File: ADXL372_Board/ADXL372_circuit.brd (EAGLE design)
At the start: 45 x 45 mm, 35 parts, among them IC4 SI7006-A20-IM, IC5 LP5907MFX-2.5/NOPB, SW1 DHT-4235A, U1 MX25R1635FM1IL0, U2 ADXL345BCCZ, U3 ADXL372BCCZ-RL7, Y1 16MHZ_X053201602002, Y2 3.2768KHZ

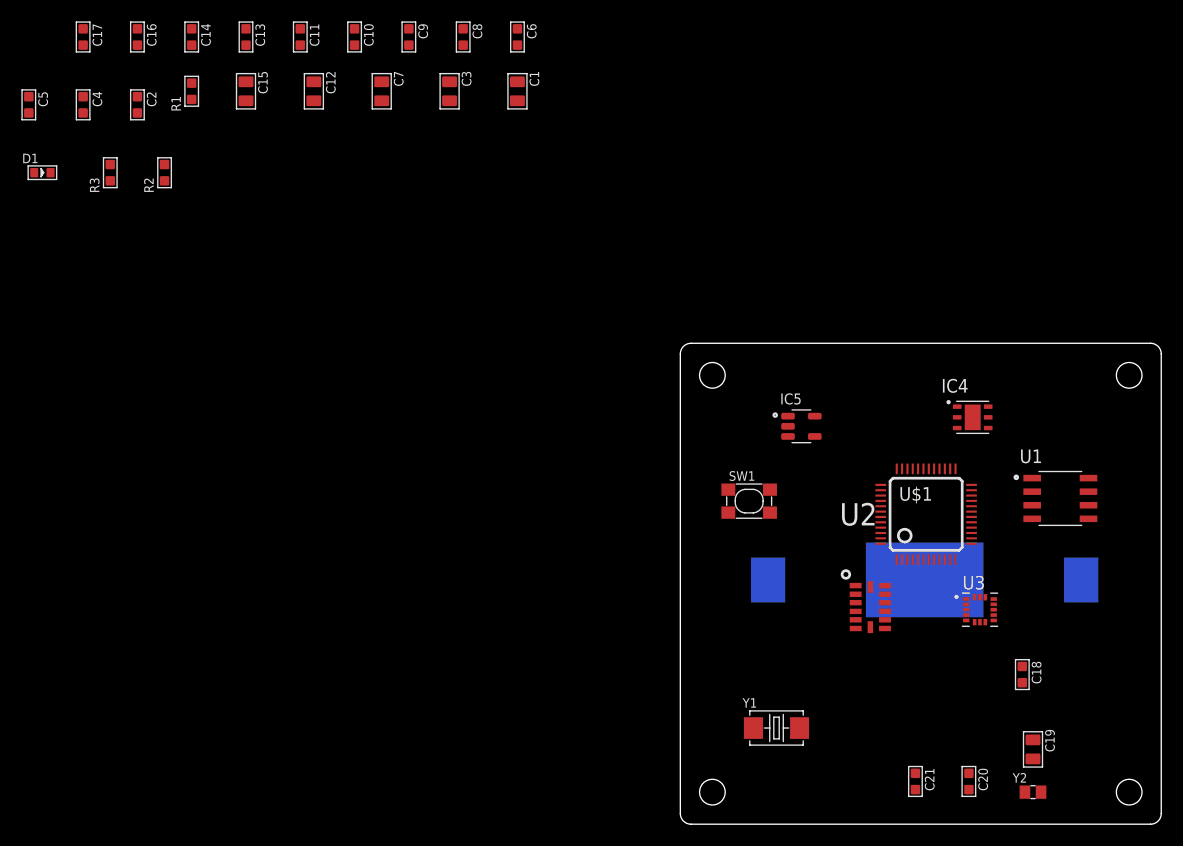
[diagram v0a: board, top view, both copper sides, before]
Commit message: 基板図面を修正
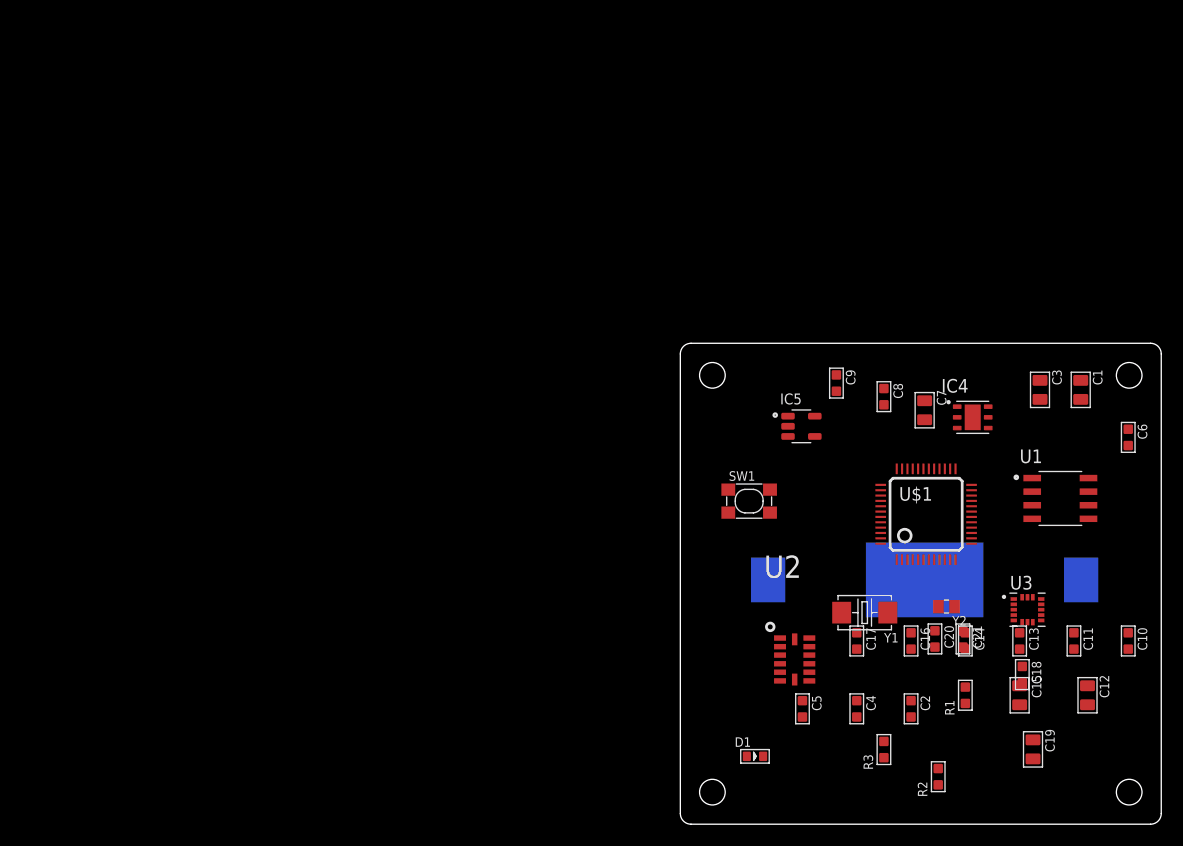
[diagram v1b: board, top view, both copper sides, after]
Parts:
- moved C10 91.8 mm to (41.9, 17.1)
- moved C11 91.8 mm to (36.8, 17.1)
- moved C12 91.8 mm to (38.1, 12.1)
- moved C13 91.8 mm to (31.8, 17.1)
- moved C14 91.8 mm to (26.7, 17.1)
- moved C15 91.8 mm to (31.8, 12.1)
- moved C16 91.8 mm to (21.6, 17.1)
- moved C17 91.8 mm to (16.5, 17.1)
- moved C2 91.8 mm to (21.6, 10.8)
- moved C4 91.8 mm to (16.5, 10.8)
- moved C5 91.8 mm to (11.4, 10.8)
- moved R1 91.8 mm to (26.7, 12.1)
- moved R2 91.8 mm to (24.1, 4.45)
- moved R3 90.3 mm to (19.1, 6.99)
- moved D1 86.2 mm to (6.99, 6.35)
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
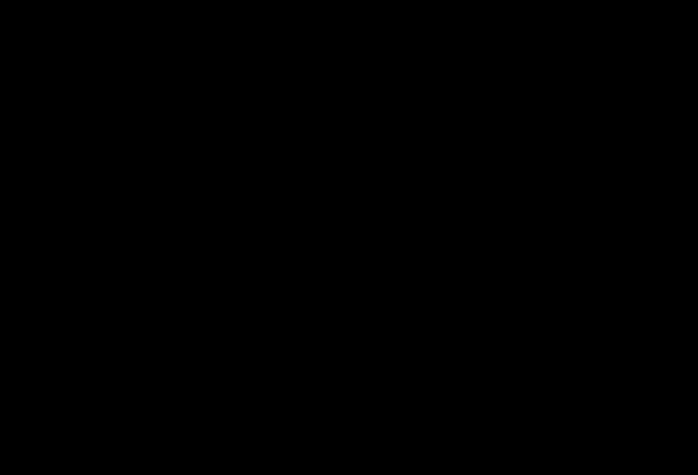
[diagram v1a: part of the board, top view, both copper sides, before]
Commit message: LED駆動用FETを追加
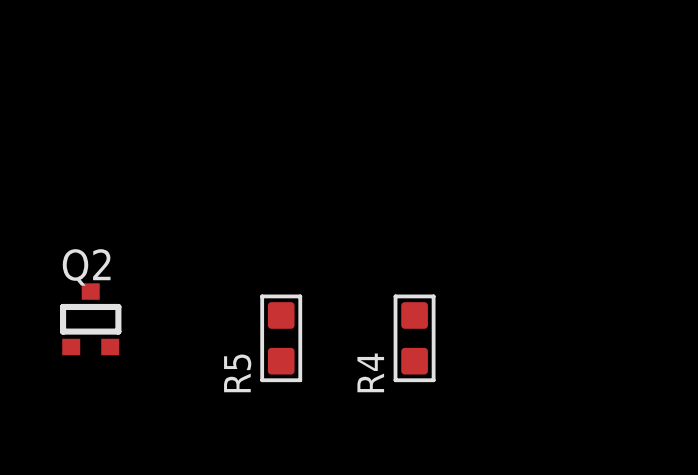
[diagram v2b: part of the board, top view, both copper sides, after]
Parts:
- added Q2: BSS138W, BSS138W:SOT323-R
- added R4: 100k, OPL_Resistor:R0603
- added R5: 100, OPL_Resistor:R0603
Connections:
- new net N$17: R5.2, U$1.10
- new net N$20: Q2.1, R4.2, R5.1
- new net VCC: C15.2, C7.2, IC5.5
- net +2V5: no longer C15.2, C7.2, IC5.5
- net +3V3: now also R1.2
- net GND: now also Q2.2, R4.1; no longer D1.-
- net N$19: now also D1.-, Q2.3; no longer R1.2, U$1.10

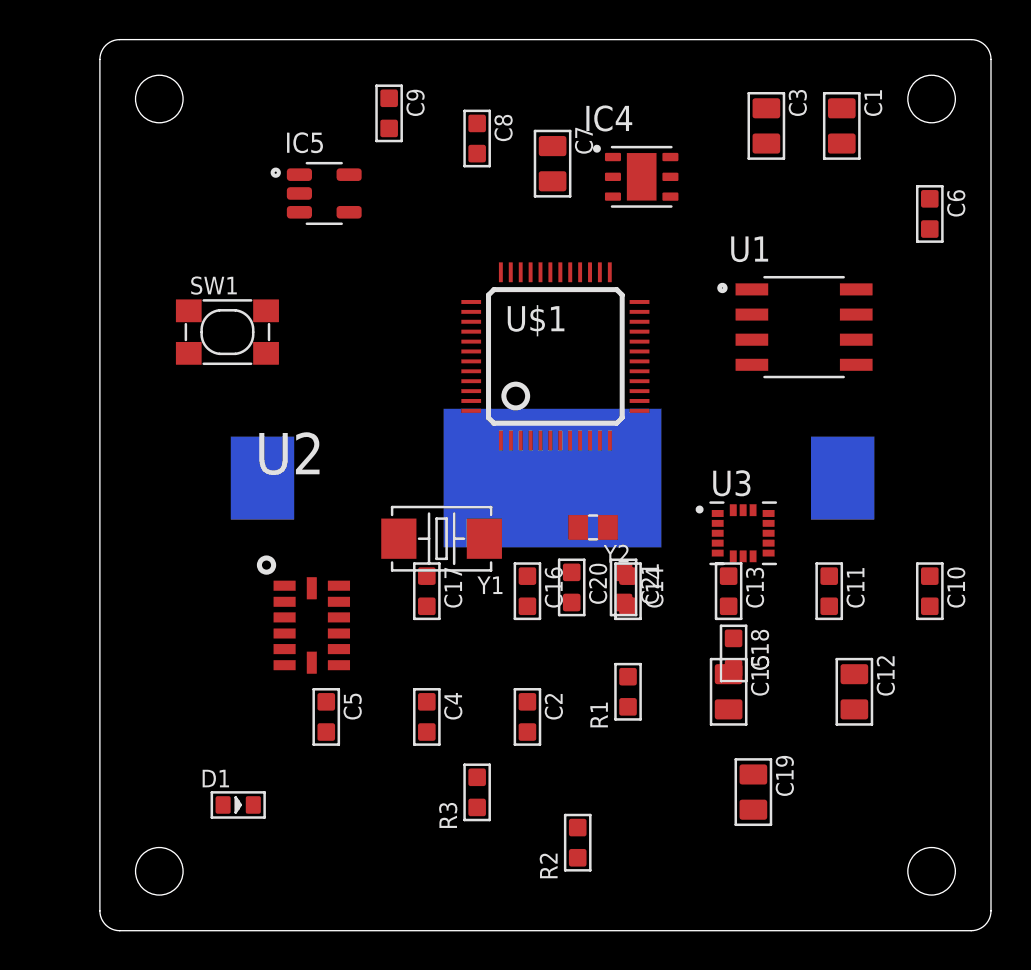
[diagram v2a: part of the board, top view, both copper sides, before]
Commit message: パターン図を修正
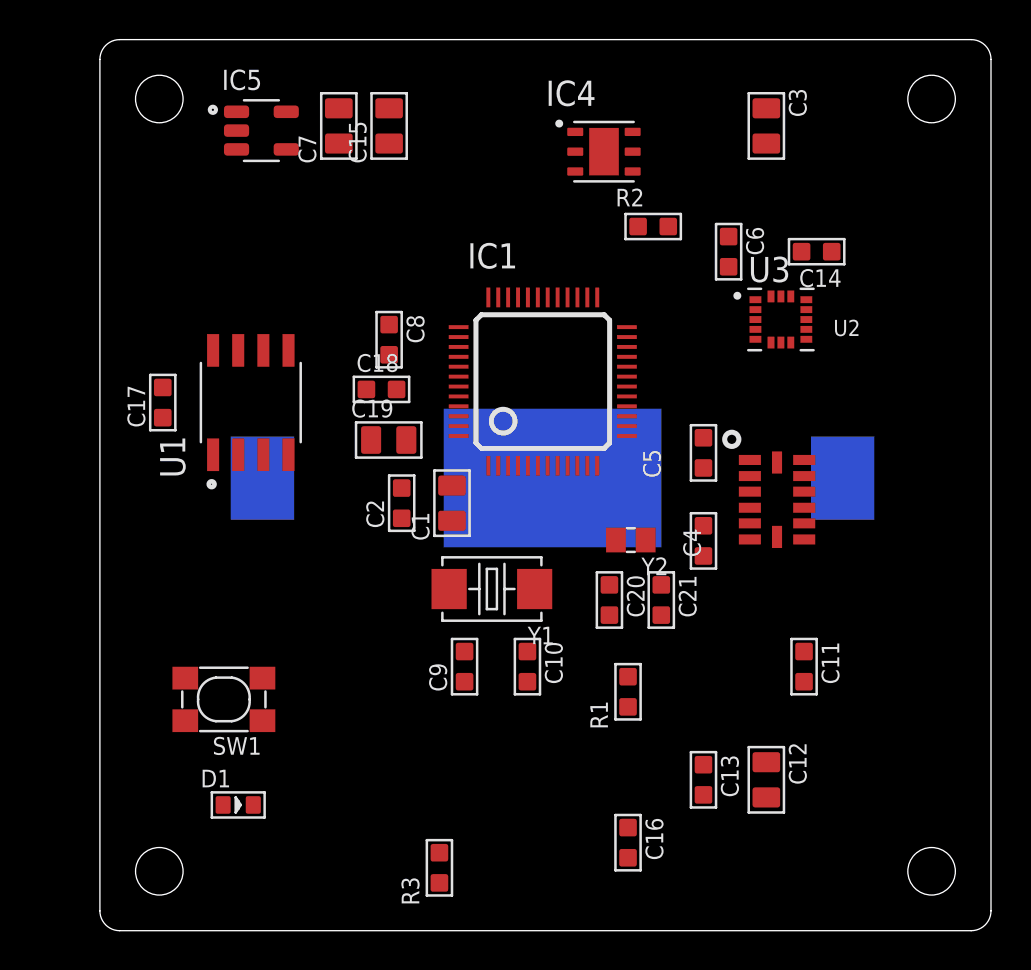
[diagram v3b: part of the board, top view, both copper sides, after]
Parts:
- removed U$1: STM32L051C6, stm32l05x6:LQFP48
- added IC1: STM32L051C6, stm32l05x6:LQFP48
- moved C15 33.3 mm to (14.6, 40.6), turned to 180 degrees
- moved R2 31.3 mm to (27.9, 35.6), turned to 270 degrees
- moved U1 28.2 mm to (7.62, 26.7), turned to 90 degrees
- moved C9 28.2 mm to (18.4, 13.3), turned to 180 degrees
- moved C1 27.4 mm to (17.8, 21.6), turned to 180 degrees
- moved C19 25.6 mm to (14.6, 24.8), turned to 90 degrees
- moved U2 24.3 mm to (34.2, 21.8)
- moved C5 23.3 mm to (30.5, 24.1), turned to 180 degrees
- moved C18 22.2 mm to (14.2, 27.3), turned to 90 degrees
- moved C10 20.7 mm to (21.6, 13.3)
- moved C14 19.6 mm to (36.2, 34.3), turned to 270 degrees
- moved SW1 18.6 mm to (6.26, 11.7), turned to 180 degrees
- moved C4 16.6 mm to (30.5, 19.7)
- moved C17 16.4 mm to (3.17, 26.7), turned to 180 degrees
- moved C16 13.7 mm to (26.7, 4.45)
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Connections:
- net +2V5: now also IC1.1, IC1.36, IC1.48, IC1.9; no longer U$1.1, U$1.36, U$1.48, U$1.9
- net ADXL345_CS: now also IC1.29; no longer U$1.29
- net ADXL372_CS: now also IC1.30; no longer U$1.30
- net GND: now also IC1.23, IC1.35, IC1.47; no longer U$1.23, U$1.35, U$1.47
- net I2C1_SCL: now also IC1.45; no longer U$1.45
- net I2C1_SDA: now also IC1.46; no longer U$1.46
- net I2C2_SCL: now also IC1.26; no longer U$1.26
- net I2C2_SDA: now also IC1.27; no longer U$1.27
- net N$1: now also IC1.3; no longer U$1.3
- net N$14: now also IC1.5; no longer U$1.5
- net N$15: now also IC1.6; no longer U$1.6
- net N$16: now also IC1.31; no longer U$1.31
- net N$17: now also IC1.10; no longer U$1.10
- net N$2: now also IC1.4; no longer U$1.4
- net N$3: now also IC1.7; no longer U$1.7
- net SPI1_MISO: now also IC1.16; no longer U$1.16
- net SPI1_MOSI: now also IC1.17; no longer U$1.17
- net SPI1_SCK: now also IC1.15; no longer U$1.15

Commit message: 回路図修正
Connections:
- removed net N$16: IC1.31
- removed net N$24: U1.1
- removed net N$5: U3.4
- removed net N$6: U3.8
- removed net N$7: U3.6
- removed net N$8: U3.7
- new net FLASH_MEMORY: IC1.31, U1.1
- net ADXL372_CS: now also U3.8
- net SPI1_MISO: now also U3.7
- net SPI1_MOSI: now also U3.6
- net SPI1_SCK: now also U3.4

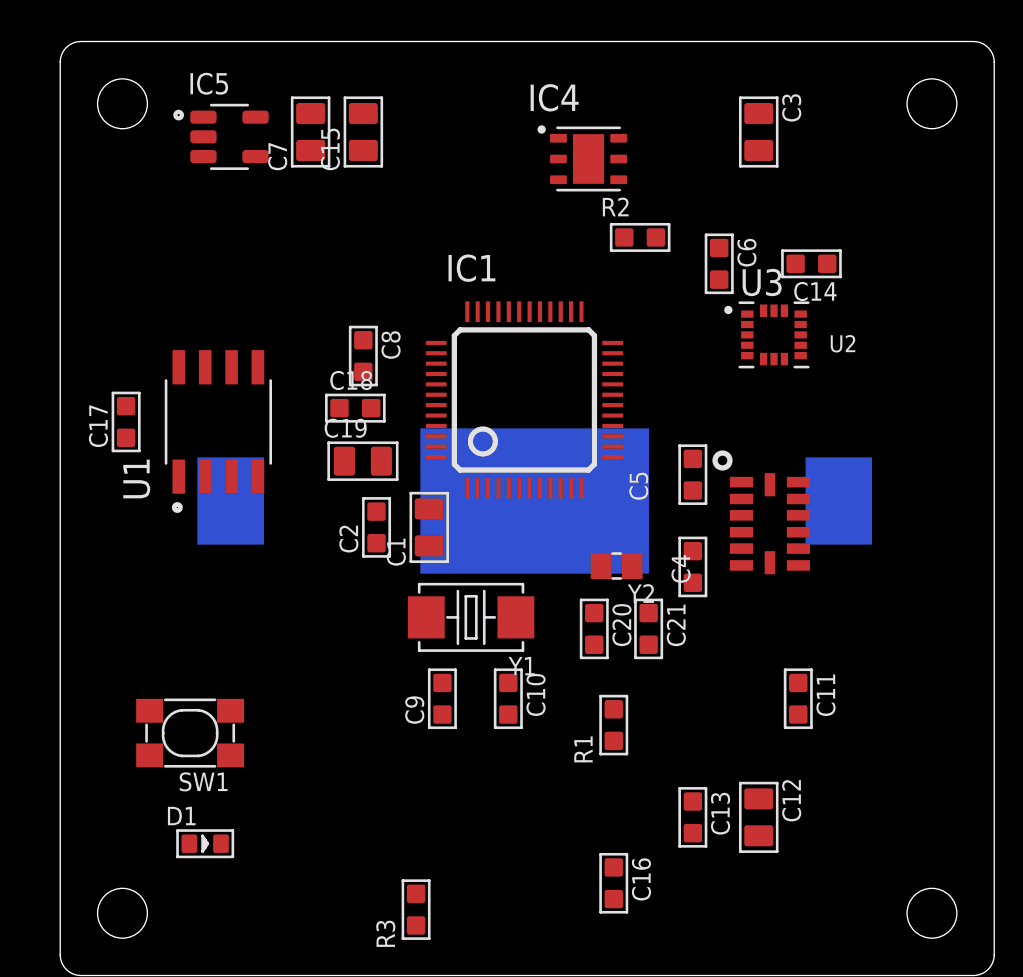
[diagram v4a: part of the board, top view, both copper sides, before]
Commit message: パターン図を修正
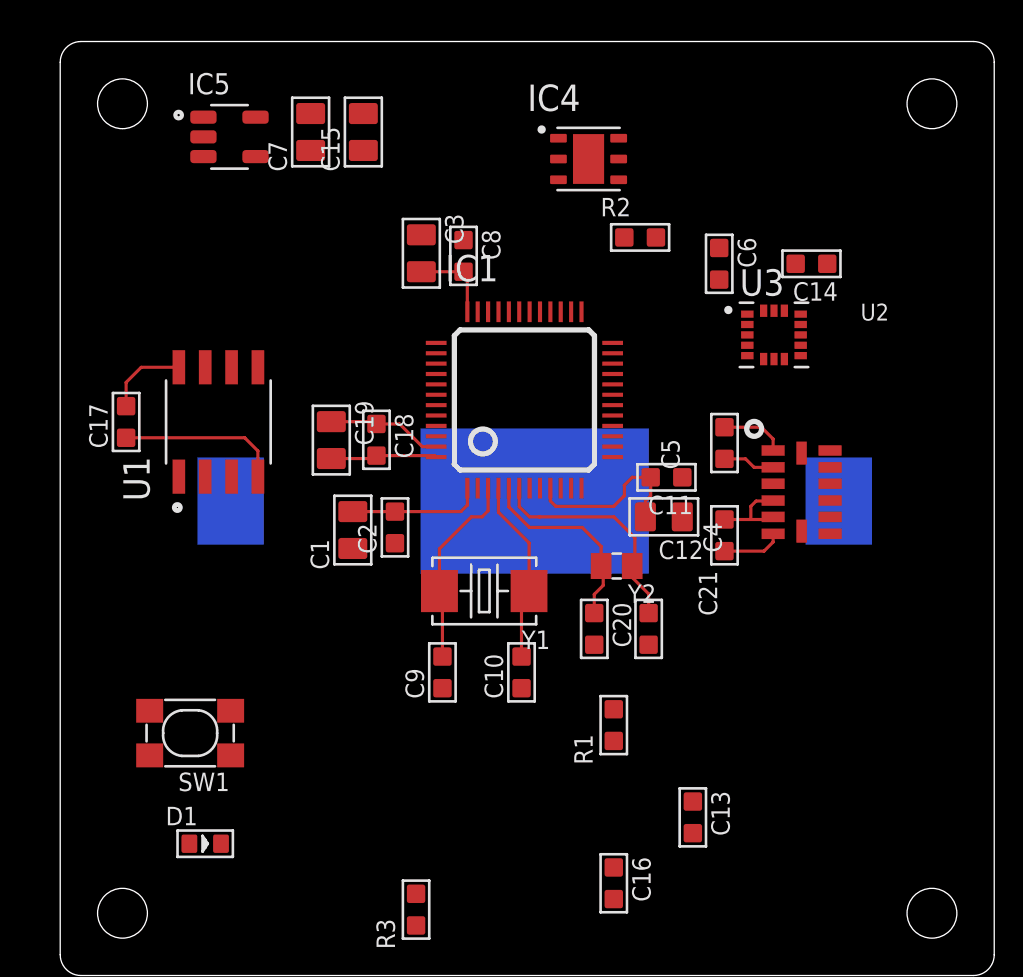
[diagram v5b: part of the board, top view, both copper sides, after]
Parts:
- moved C3 17.3 mm to (17.4, 34.8)
- moved C12 15.2 mm to (29.1, 22.1), turned to 270 degrees
- moved C11 12.4 mm to (29.2, 24.0), turned to 270 degrees
- moved C8 6.82 mm to (19.4, 34.7)
- moved C1 3.69 mm to (14.1, 21.5)
- moved U2 2.16 mm to (35.7, 23.3)
- moved C4 2.16 mm to (32.0, 21.2)
- moved C5 2.16 mm to (32.0, 25.7)
- moved C18 1.83 mm to (15.2, 25.8), turned to 0 degrees
- moved C19 1.83 mm to (13.1, 25.8), turned to 0 degrees
- moved C10 1.42 mm to (22.2, 14.6), turned to 180 degrees
- moved Y1 1.42 mm to (20.4, 18.5)
- moved C9 1.27 mm to (18.4, 14.6)
- moved C2 0.89 mm to (16.1, 21.6)
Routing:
- net +2V5: track 0.00 -> 24.1 mm
- net GND: track 0.00 -> 20.1 mm
- net N$15: track 0.00 -> 11.3 mm
- net +3V3: track 0.00 -> 10.0 mm
- net N$14: track 0.00 -> 9.57 mm
- net N$1: track 0.00 -> 9.44 mm
- net N$2: track 0.00 -> 8.87 mm

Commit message: Update circuit
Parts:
- added CN1: FH12-08S-1SH, con-hirose:FH12-08S-1SH
- moved Q2 32.6 mm to (12.2, 5.46)
- moved R5 29.5 mm to (15.2, 6.35)
- moved R4 28.3 mm to (17.9, 9.40)
- moved C16 9.57 mm to (35.6, 8.00)
- moved R3 8.07 mm to (13.8, 10.5)
- renumbered U1 to IC6, U2 to IC2, U3 to IC3
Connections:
- removed net N$10: IC2.13
- removed net N$11: IC2.12
- removed net N$17: IC1.10, R5.2
- removed net N$20: Q2.1, R4.2, R5.1
- removed net N$9: IC2.7
- new net SPI1_NSS: IC1.14
- new net SPI2_MISO: IC1.27, IC6.2
- new net SPI2_MOSI: IC1.28, IC6.5
- new net SPI2_NSS: IC1.25
- new net SPI2_SCK: IC1.26, IC6.6
- new net USART1_CK: CN1.3, IC1.29
- new net USART1_RX: CN1.5, IC1.31
- new net USART1_TX: CN1.4, IC1.30
- net +2V5: now also C14.2, C6.2, IC3.1, IC3.14
- net +3V3: now also CN1.1, CN1.2; no longer C14.2, C6.2, IC3.1, IC3.14
- net ADXL345_CS: now also IC1.12, IC2.7; no longer IC1.29
- net ADXL372_CS: now also IC1.13; no longer IC1.30
- net FLASH_MEMORY: now also IC1.22; no longer IC1.31
- net GND: now also CN1.7, CN1.8
- net I2C2_SCL: no longer IC1.26
- net I2C2_SDA: no longer IC1.27
- net N$22: now also IC5.3
- net N$4: now also Q2.1, R4.2, R5.2; no longer IC2.14
- net SPI1_MISO: now also IC2.12; no longer IC6.2
- net SPI1_MOSI: now also IC2.13; no longer IC6.5
- net SPI1_SCK: now also IC2.14; no longer IC6.6

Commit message: update circuit
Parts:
- removed BT1: BU2032SM-HD-G, BU2032SM-HD-G:BAT_BU2032SM-HD-G
- removed C15, C7: 10uf, OPL_Capacitor:C0805
- removed IC5: LP5907MFX-2.5/NOPB, LP5907MFX-2.5_NOPB:SOT95P280X145-5N
- added BT2: BU2032SM-HD-G, BU2032SM-HD-G:BAT_BU2032SM-HD-G
- added C22, C24, C25: 10uf, OPL_Capacitor:C0805
- added C23: 100nf, OPL_Capacitor:C0603
- added IC7: 74AHC1G14DCK, 74xx-little-us:SC70-5
- added IC8: LP5907MFX-2.5/NOPB, LP5907MFX-2.5_NOPB:SOT95P280X145-5N
- added R6: 10K 1/10W, OPL_Resistor:R0603
- added SW2: B3U-1000P-2P-SMD, OPL_Switch:SW2-2.6-3.0X2.5X1.2+0.4MM
- added SW3: JS202011SCQN, JS202011SCQN:SW_JS202011SCQN
- added TP1, TP2, TP3, TP4, TP5, TP6, TP7, TP8: TPB1,27, testpad:B1,27
- moved IC4 31.2 mm to (4.80, 15.9), turned to 270 degrees
- moved R2 29.1 mm to (8.38, 14.0), turned to 0 degrees
- moved SW1 28.2 mm to (10.1, 39.6)
- moved R3 9.09 mm to (8.51, 17.9), turned to 180 degrees
- moved C14 8.10 mm to (41.5, 28.2)
- moved R4 7.58 mm to (10.5, 11.2)
- moved C5 5.93 mm to (33.0, 19.8)
- moved IC2 5.43 mm to (36.7, 18.0)
- moved C4 5.43 mm to (33.0, 15.9)
- moved Y1 5.43 mm to (19.4, 13.2)
- moved C10 5.30 mm to (20.7, 9.53)
- moved C9 5.09 mm to (18.2, 9.53)
- moved Q2 4.60 mm to (8.00, 7.37), turned to 90 degrees
- moved C21 4.26 mm to (27.1, 12.6)
- moved C20 4.19 mm to (24.7, 12.6)
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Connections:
- removed net N$12: IC3.11
- removed net N$13: IC3.9
- removed net N$22: BT1.+, IC5.1, IC5.3
- new net +BAT: BT2.+, SW3.1, SW3.4
- new net +VIN: IC8.1, IC8.3, SW3.2, SW3.5
- new net 345_INT1: IC1.11, IC2.8
- new net 345_INT2: IC1.12, IC2.9
- new net 372_INT1: IC1.19, IC3.11
- new net 372_INT2: IC1.20, IC3.9
- new net MODE_LED: IC1.39, R5.1
- new net MODE_SW: IC1.40, IC7.4
- new net N$10: IC1.43, TP7.TP
- new net N$11: IC1.21, TP8.TP
- new net N$5: IC7.2, R6.1, SW2.2
- new net N$6: IC1.13, TP3.TP
- new net N$7: IC1.38, TP4.TP
- new net N$8: IC1.41, TP5.TP
- new net N$9: IC1.42, TP6.TP
- new net SYS_SWCLK: IC1.37, TP2.TP
- new net SYS_SWDIO: IC1.34, TP1.TP
- new net USART1_CTS: CN1.5, IC1.32
- new net USART1_RTS: CN1.6, IC1.33
- net +2V5: now also C22.2
- net +3V3: now also C23.2, IC7.5, R6.2, SW3.3, SW3.6; no longer CN1.2
- net ADXL345_CS: now also IC1.10; no longer IC1.12
- net ADXL372_CS: now also IC1.18; no longer IC1.13
- net GND: now also BT2.-, C22.1, C23.1, C24.1, C25.1, IC7.3, IC8.2, SW2.1; no longer BT1.-, C15.1, C7.1, IC5.2
- net USART1_CK: now also CN1.2; no longer CN1.3
- net USART1_RX: now also CN1.4; no longer CN1.5
- net USART1_TX: now also CN1.3; no longer CN1.4
- net VCC: now also C24.2, C25.2, IC8.5; no longer C15.2, C7.2, IC5.5
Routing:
- net SPI2_MISO: track 0.00 -> 34.2 mm, vias 0 -> 2
- net FLASH_MEMORY: track 0.00 -> 28.9 mm, vias 0 -> 2
- net SPI2_SCK: track 0.00 -> 26.3 mm, vias 0 -> 2
- net 345_INT2: track 0.00 -> 23.6 mm, vias 0 -> 2
- net 345_INT1: track 0.00 -> 23.4 mm, vias 0 -> 2
- net SPI2_MOSI: track 0.00 -> 20.9 mm, vias 0 -> 2
- net ADXL345_CS: track 0.00 -> 19.3 mm, vias 0 -> 2
- net SPI1_MISO: track 0.00 -> 18.7 mm
- net SPI1_SCK: track 0.00 -> 17.6 mm, vias 0 -> 2
- net SPI1_MOSI: track 0.00 -> 16.8 mm, vias 0 -> 2
- net SYS_SWDIO: track 0.00 -> 13.7 mm, vias 0 -> 2
- net 372_INT2: track 0.00 -> 11.9 mm, vias 0 -> 2
- net USART1_CK: track 0.00 -> 11.3 mm
- net USART1_TX: track 0.00 -> 11.1 mm
- net USART1_RX: track 0.00 -> 10.9 mm
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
